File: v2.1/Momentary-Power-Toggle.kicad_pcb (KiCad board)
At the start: 2 copper layers, 12.9 x 9 mm, 13 parts, among them Q1 IRF7317PbF

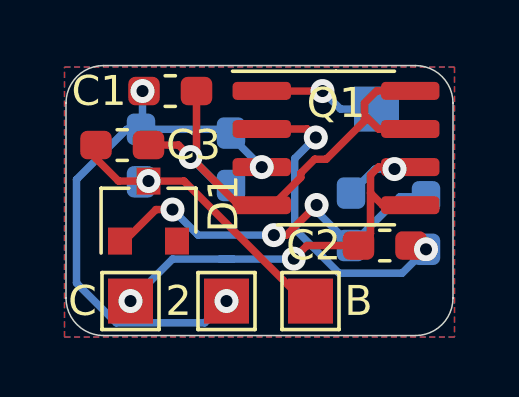
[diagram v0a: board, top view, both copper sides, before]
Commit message: cleanup
cleaned up readme, board files, added renders, made small tweaks to some of the boards (added identifiers and changed labels for consistency)
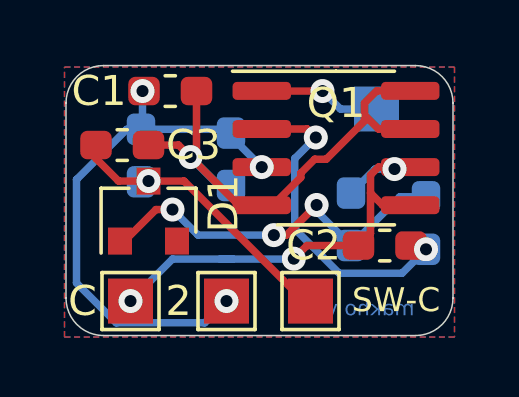
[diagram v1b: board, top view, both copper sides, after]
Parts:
- renumbered B to SW-C
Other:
- board text added: "https://github.com /makhowastaken /Soft-Latching-Power-Button"
- board text added: "makho v2.1"
